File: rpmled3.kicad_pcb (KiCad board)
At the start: 2 copper layers, 49 x 82 mm, 41 parts, among them J1 Conn_01x02, J2 Conn_01x04, J3 Conn_01x02, J4 Conn_01x02, J7 Conn_01x02, U1 STP16C596, U2 STM32F042K6Tx, U3 STP16C596, U4 SN65HVD230, U5 ST1S14PHR_MY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

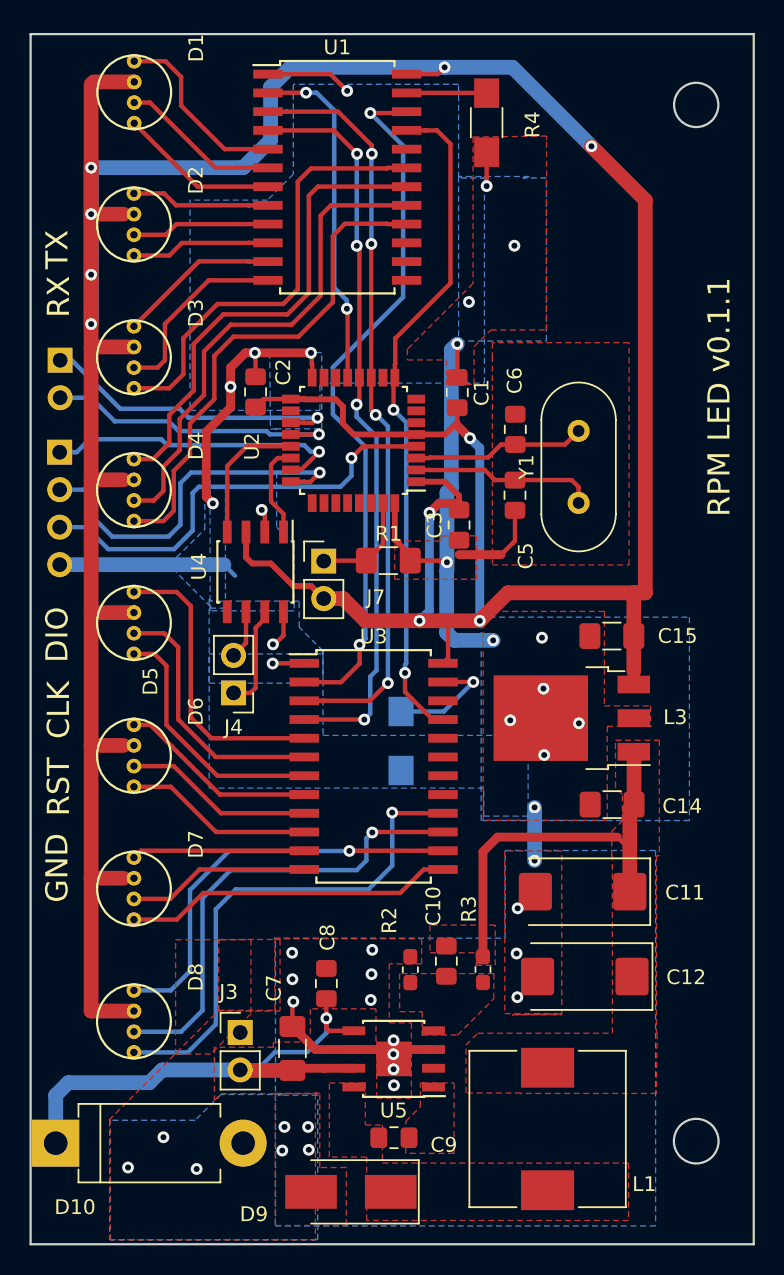
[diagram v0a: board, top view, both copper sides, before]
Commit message: Не стандартные компоненты перенесены в локальную библиотеку Исправления v0.1.2
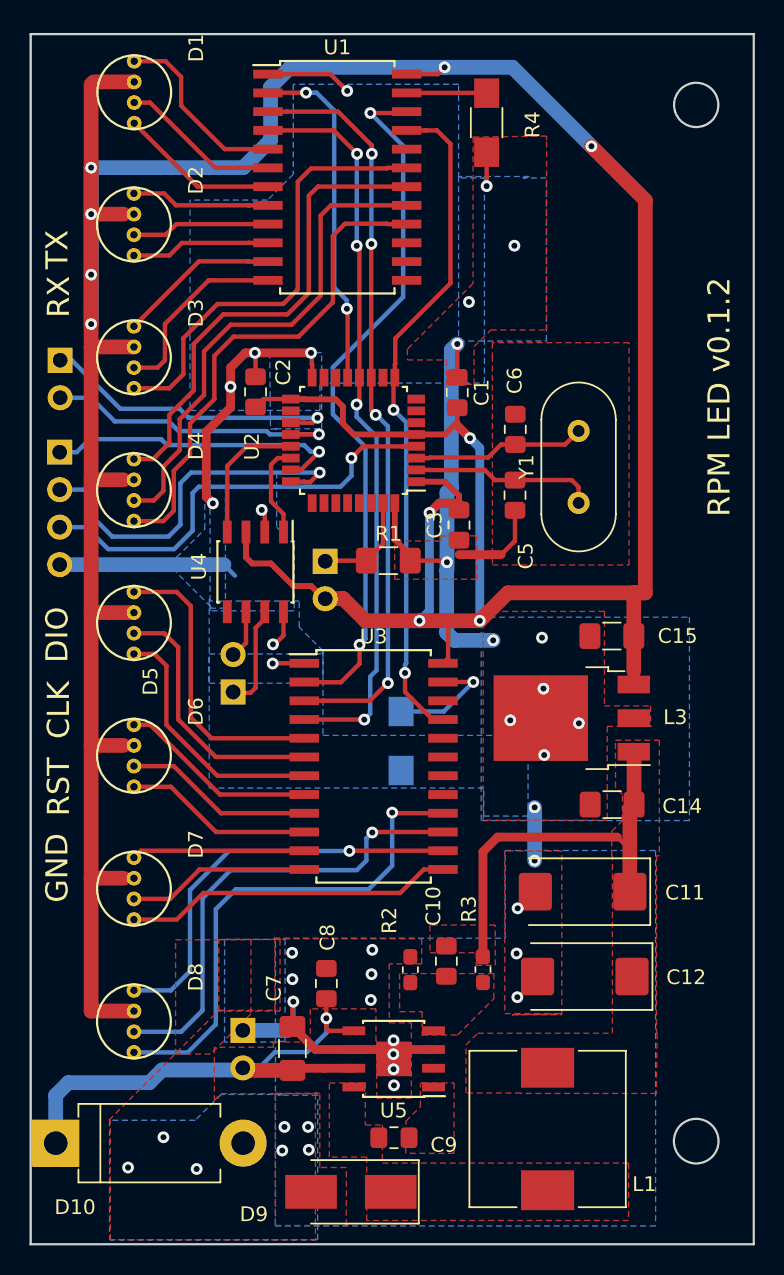
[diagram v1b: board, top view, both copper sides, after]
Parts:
- D1, D2, D3, D4, D5, D6, D7, D8: footprint posad:RGB_LEB_InLine -> rpmledlib:RGB_LEB_InLine
- J3, J4, J7: moved to B.Cu
- moved J3 0.23 mm to (110.4, 145.5), turned to 180 degrees
- moved J7 0.10 mm to (116.0, 113.7), turned to 180 degrees
- moved J4 0.07 mm to (109.7, 122.6), turned to 0 degrees
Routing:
- net GND: track 99.9 -> 105.1 mm
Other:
- board text added: "RPM LED v0.1.2"
- board text removed: "RPM LED v0.1.1"
